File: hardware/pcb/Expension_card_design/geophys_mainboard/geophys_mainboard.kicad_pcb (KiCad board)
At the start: 4 copper layers, 190 x 110 mm, 297 parts, among them J1 550910274, J2 USB_C_Receptacle_USB2.0_16P, J3 550910274, J4 Micro_SD_CARD, Q1 AO3400A, Q2 AO3401A, Q3 AO3400A, U1 TPS61170, U10 TPS54331DR, U11 TPS7A2033PDBVR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

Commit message: SCL3300 driver functionnal
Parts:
- removed the D4 at (243.6, 58.8)
- removed D5, D6, D7: H5VUD5BB, Diode_SMD:D_SOD-523
- removed the Q1 at (211.8, 43.9)
- U9: value TPS25210LRPWR -> TPS2116DRL; footprint magnode_footprints:SMD_VQFN-HR-10 -> Package_TO_SOT_SMD:SOT-583-8
- moved U9 10.0 mm to (203.6, 77.5), turned to 0 degrees
- moved J2 0.11 mm to (236.6, 53.1)
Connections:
- D3 pad 1: /DATA_SAVING/CC2 -> /DATA_SAVING/+5VBUS
- D3 pad 3: /DATA_SAVING/CC1 -> /DATA_SAVING/D-
- D3 pad 4: unconnected-(D3-L3-Pad4) -> /DATA_SAVING/D+
- D3 pad 5: unconnected-(D3-L4-Pad5) -> /DATA_SAVING/CC1
- D3 pad 6: /DATA_SAVING/+5VBUS -> /DATA_SAVING/CC2
- J2 pad A5: /DATA_SAVING/CC1 -> /DATA_SAVING/CC2
- J2 pad B5: /DATA_SAVING/CC2 -> /DATA_SAVING/CC1
- U9 pad 1: /PWR_3V3D/3V3D_EFUSE_EN_ULVO -> unconnected-(U9-GND-Pad1)
- U9 pad 2: unconnected-(U9-OVCSEL-Pad2) -> Net-(U9-VOUT-Pad2)
- U9 pad 4: /PWR_3V3D/3V3D_EFUSE_PGTH -> unconnected-(U9-PR1-Pad4)
- U9 pad 5: /PWR_3V3D/+5V_IN -> unconnected-(U9-MODE-Pad5)
- U9 pad 6: /PWR_3V3D/5V_HOLDUP_DIODE -> unconnected-(U9-VIN2-Pad6)
- U9 pad 7: /PWR_3V3D/3V3D_EFUSE_DVDT -> Net-(U9-VOUT-Pad2)
- U9 pad 8: GND -> unconnected-(U9-ST-Pad8)
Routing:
- net /DATA_SAVING/CC2: track 12.9 -> 1.66 mm
- net /DATA_SAVING/D-: track 25.0 -> 16.5 mm, vias 2 -> 0
- net /DATA_SAVING/CC1: track 8.43 -> 1.65 mm
- net /DATA_SAVING/D+: track 23.3 -> 17.5 mm
- net /DATA_SAVING/+5VBUS: track 31.7 -> 26.8 mm, vias 6 -> 4
- net GND: track 89.3 -> 85.5 mm, vias 503 -> 494
- net unconnected-(J2-SBU2-PadB8): track 2.56 -> 0.00 mm, vias 1 -> 0

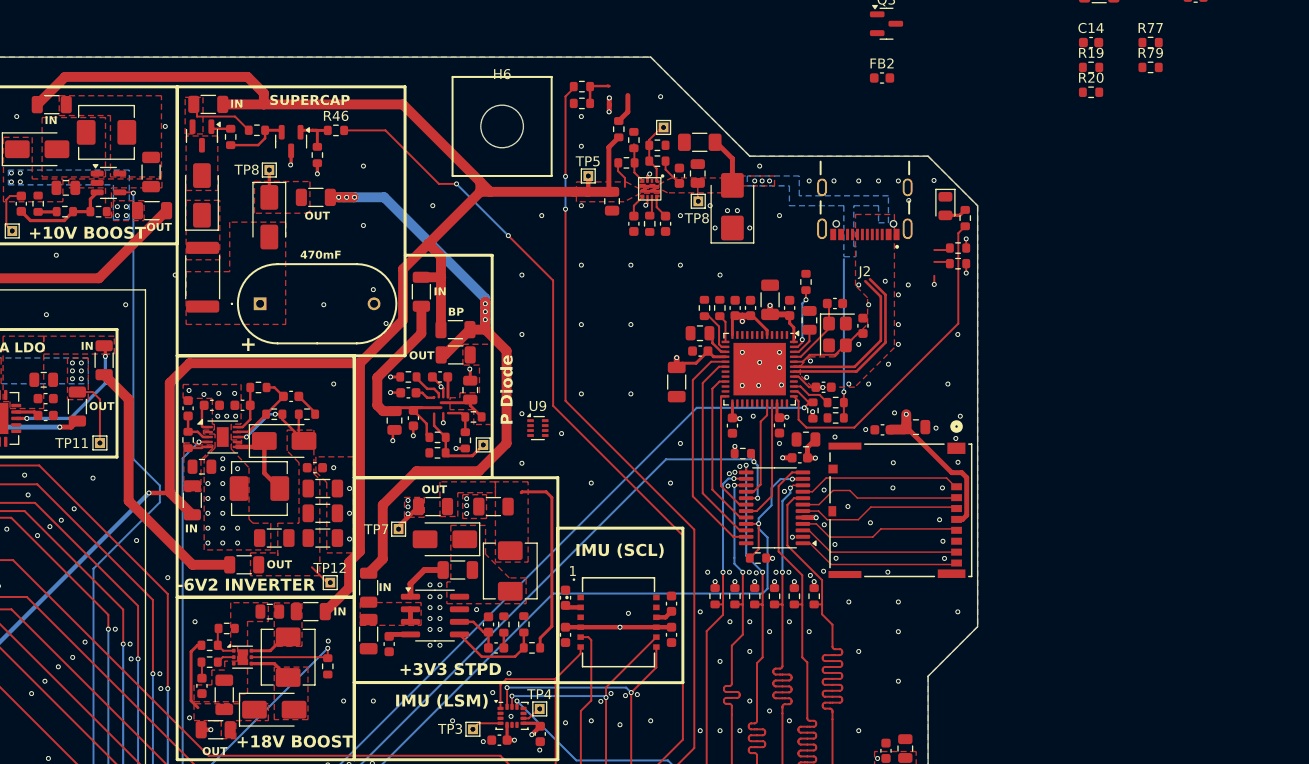
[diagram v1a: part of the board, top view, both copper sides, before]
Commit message: Backup avant deletion offset/dac
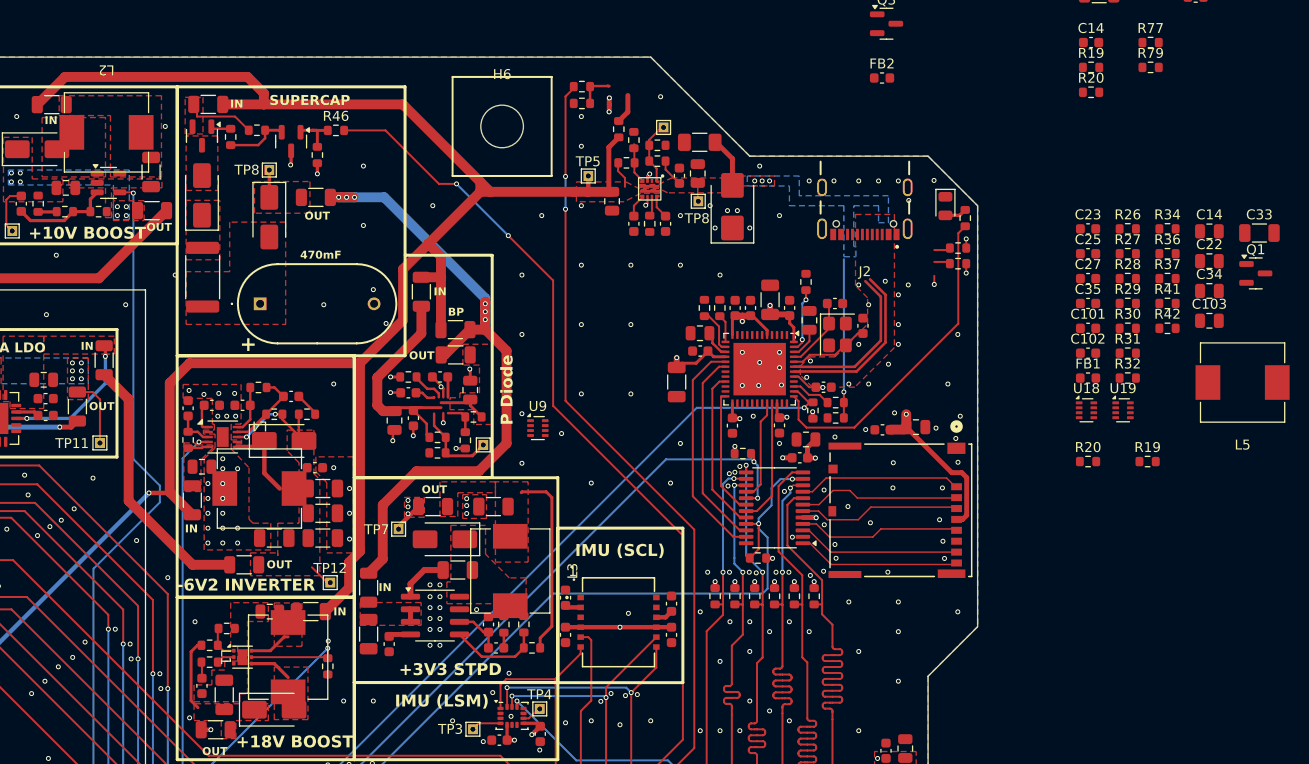
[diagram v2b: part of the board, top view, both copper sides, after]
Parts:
- added C101: 100n, Capacitor_SMD:C_0603_1608Metric, F.Cu at (259.1, 67.4)
- added C102: 100n, Capacitor_SMD:C_0603_1608Metric, F.Cu at (259.1, 69.9)
- added C103: 1u, Capacitor_SMD:C_0805_2012Metric, F.Cu at (271.4, 66.6)
- added C14: 1u, Capacitor_SMD:C_0805_2012Metric, F.Cu at (271.4, 57.6)
- added C22: 10u, Capacitor_SMD:C_0805_2012Metric, F.Cu at (271.4, 60.6)
- added C23: 100n, Capacitor_SMD:C_0603_1608Metric, F.Cu at (259.1, 57.3)
- added C25: 100n, Capacitor_SMD:C_0603_1608Metric, F.Cu at (259.1, 59.8)
- added C27: 15p, Capacitor_SMD:C_0603_1608Metric, F.Cu at (259.1, 62.4)
- added C33: 47u, Capacitor_SMD:C_1206_3216Metric, F.Cu at (276.4, 57.8)
- added C34: 10u, Capacitor_SMD:C_0805_2012Metric, F.Cu at (271.4, 63.6)
- added C35: 22n, Capacitor_SMD:C_0603_1608Metric, F.Cu at (259.1, 64.9)
- added FB1: 120Ω@100MHz 2A 50mΩ, Inductor_SMD:L_0603_1608Metric, F.Cu at (259.1, 72.4)
- added L5: 10u, magnode_footprints:ZEMS0850-100M_8.5x8.0mm, F.Cu at (274.8, 72.8)
- added Q1: AO3400A, Package_TO_SOT_SMD:SOT-23, F.Cu at (276.1, 61.8)
- added R19: 10k, Resistor_SMD:R_0603_1608Metric, F.Cu at (265.2, 80.8)
- added R20: 10k, Resistor_SMD:R_0603_1608Metric, F.Cu at (259.1, 80.8)
- added R26: 100, Resistor_SMD:R_0603_1608Metric, F.Cu at (263.2, 57.3)
- added R27: 100, Resistor_SMD:R_0603_1608Metric, F.Cu at (263.2, 59.8)
- added R28: 100k, Resistor_SMD:R_0603_1608Metric, F.Cu at (263.2, 62.4)
- added R29: 100k, Resistor_SMD:R_0603_1608Metric, F.Cu at (263.2, 64.9)
- added R30: 300k, Resistor_SMD:R_0603_1608Metric, F.Cu at (263.2, 67.4)
- added R31: 100k, Resistor_SMD:R_0603_1608Metric, F.Cu at (263.2, 69.9)
- added R32: 300k, Resistor_SMD:R_0603_1608Metric, F.Cu at (263.2, 72.4)
- added R34: 300k, Resistor_SMD:R_0603_1608Metric, F.Cu at (267.2, 57.3)
- added R36: ~, Resistor_SMD:R_0603_1608Metric, F.Cu at (267.2, 59.8)
- added R37: 300k, Resistor_SMD:R_0603_1608Metric, F.Cu at (267.2, 62.4)
- added R41: 100k, Resistor_SMD:R_0603_1608Metric, F.Cu at (267.2, 64.9)
- added R42: 100k, Resistor_SMD:R_0603_1608Metric, F.Cu at (267.2, 67.4)
- added U18: TPS2116DRL, Package_TO_SOT_SMD:SOT-583-8, F.Cu at (259.0, 75.7)
- added U19: TPS62933, Package_TO_SOT_SMD:SOT-583-8, F.Cu at (262.7, 75.7)
- L1, L2, L3, L4: footprint Inductor_SMD:L_Sunlord_MWSA0503S -> magnode_footprints:ZEMS0850-100M_8.5x8.0mm
- R64: value 27k -> 2k4
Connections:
- net /ADC_AD777x/PT1000_AIN+ renamed /ADC_AD777x/TH_AIN+
- net /ADC_AD777x/PT1000_AIN- renamed /ADC_AD777x/TH_AIN-
- net /ADC_AD777x/PT1000_DRAIN renamed /ADC_AD777x/TH_DRAIN
- net /PWR_3V3D/5V_SUPERCAP renamed /POWER/5V_SUPERCAP
- net /PWR_3V3D/STPD_3V3_BOOT renamed /POWER/STPD_3V3_BOOT
- net /PWR_3V3D/STPD_3V3_COMP renamed /POWER/STPD_3V3_COMP
- net /PWR_3V3D/STPD_3V3_COMP_F renamed /POWER/STPD_3V3_COMP_F
- net /PWR_3V3D/STPD_3V3_PH renamed /POWER/STPD_3V3_PH
- net /PWR_3V3D/STPD_3V3_SS renamed /POWER/STPD_3V3_SS
- net /PWR_3V3D/STPD_3V3_VSENS renamed /POWER/STPD_3V3_VSENS
- C28 pad 1: /PWR_3V3D/5V_HOLDUP_IN -> /POWER/5V_STEP_DOWN_IN
- C29 pad 1: /PWR_3V3D/+3V3_OUT -> +3V3
- D9 pad 1: Net-(D9-K) -> /POWER/5V_HOLDUP_CAP
- L3 pad 2: /PWR_3V3D/+3V3_OUT -> +3V3
- Q2 pad 2: /PWR_3V3D/+5V_SUPERCAP_IN -> +5V
- R15 pad 1: +5V -> /PWR_9V_BRIDGE/+5V
- R38 pad 1: /PWR_3V3D/+3V3_OUT -> +3V3
- R44 pad 1: /PWR_3V3D/+5V_SUPERCAP_IN -> +5V
- R50 pad 1: +5V -> /PWR_3V3A/+5V
- R91 pad 1: +5V -> /DATA_SAVING/+5VBUS
- U10 pad 2: /PWR_3V3D/5V_HOLDUP_IN -> /POWER/5V_STEP_DOWN_IN
- U10 pad 3: /PWR_3V3D/5V_HOLDUP_IN -> /POWER/5V_STEP_DOWN_IN
- U4 pad 7: /IO_CONNECTOR/EN_KEEPALIVE -> /MCU_ESP32S3/EN_KEEPALIVE
- U5 pad 10: /IMU/CS_LSM -> /IMU/SCLK
- U5 pad 11: /MCU_ESP32S3/EN_SUPERCAP_CHARGE -> /IMU/MOSI
- U5 pad 12: /IMU/MOSI -> /DEVICE_DETECT_2
- U5 pad 13: /IMU/SCLK -> /DEVICE_DETECT_1
- U5 pad 28: /DEVICE_DETECT_2 -> /MCU_ESP32S3/EN_SUPERCAP_CHARGE
- U5 pad 31: /DEVICE_DETECT_1 -> unconnected-(U5-GPIO39-Pad31)
- U9 pad 1: unconnected-(U9-GND-Pad1) -> GND
- U9 pad 2: Net-(U9-VOUT-Pad2) -> /POWER/5V_STEP_DOWN_IN
- U9 pad 3: unconnected-(U9-VIN1-Pad3) -> +5V
- U9 pad 4: unconnected-(U9-PR1-Pad4) -> Net-(U9-PR1)
- U9 pad 5: unconnected-(U9-MODE-Pad5) -> +5V
- U9 pad 6: unconnected-(U9-VIN2-Pad6) -> /POWER/5V_HOLDUP_CAP
- U9 pad 7: Net-(U9-VOUT-Pad2) -> /POWER/5V_STEP_DOWN_IN
- U9 pad 8: unconnected-(U9-ST-Pad8) -> /POWER/5V_USB_PRESENT
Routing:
- net +3V3: track 446.6 -> 465.6 mm
- net /PWR_3V3D/+3V3_OUT: track 19.0 -> 0.00 mm
- net /PWR_3V3D/5V_HOLDUP_IN: track 1.36 -> 0.00 mm
- net /POWER/5V_STEP_DOWN_IN: track 0.00 -> 1.36 mm
- added copper zone on F.Cu, net /POWER/5V_HOLDUP_CAP
- added copper zone on F.Cu, net /POWER/5V_STEP_DOWN_IN
- removed copper zone on F.Cu, net /PWR_3V3D/+3V3_OUT
- removed copper zone on F.Cu, net /PWR_3V3D/+5V_SUPERCAP_IN
- removed copper zone on F.Cu, net /PWR_3V3D/5V_HOLDUP_IN
- removed copper zone on F.Cu, net Net-(D9-K)

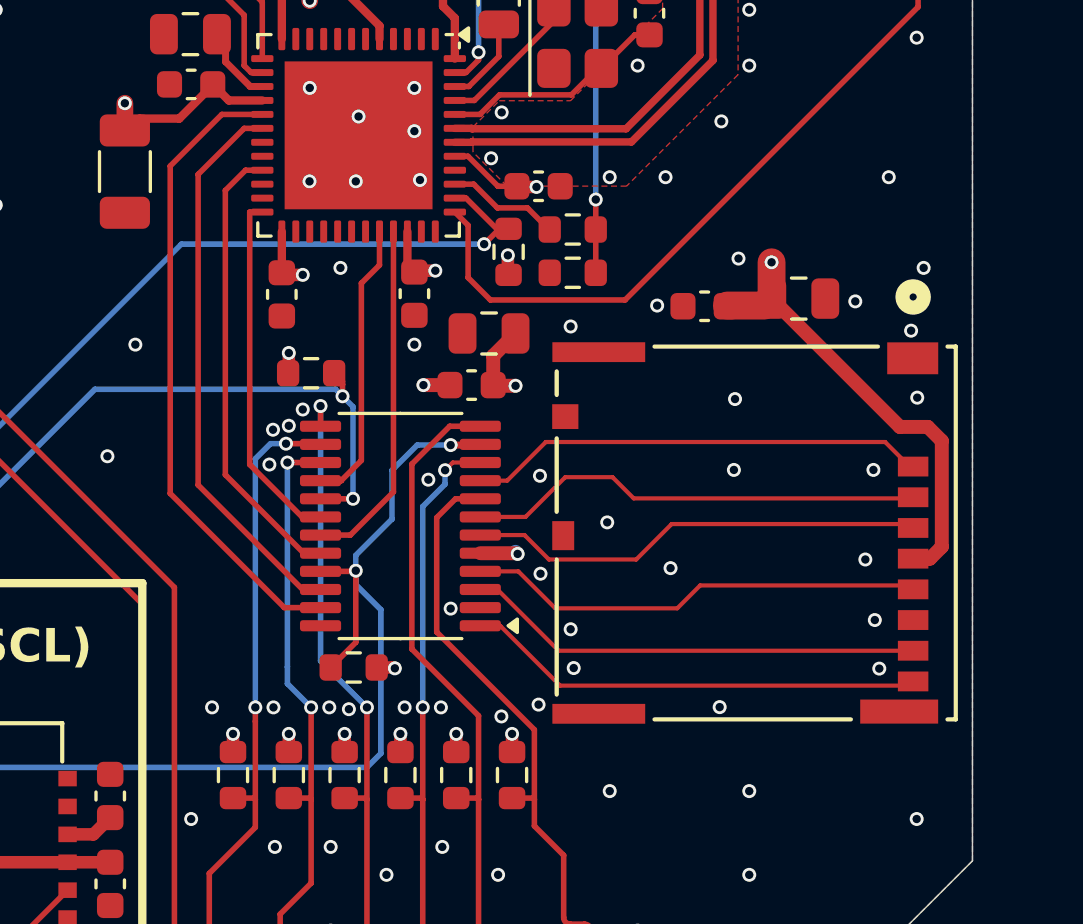
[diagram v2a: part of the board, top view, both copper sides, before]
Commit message: SD mux and 3V3D power sequencing bring-up
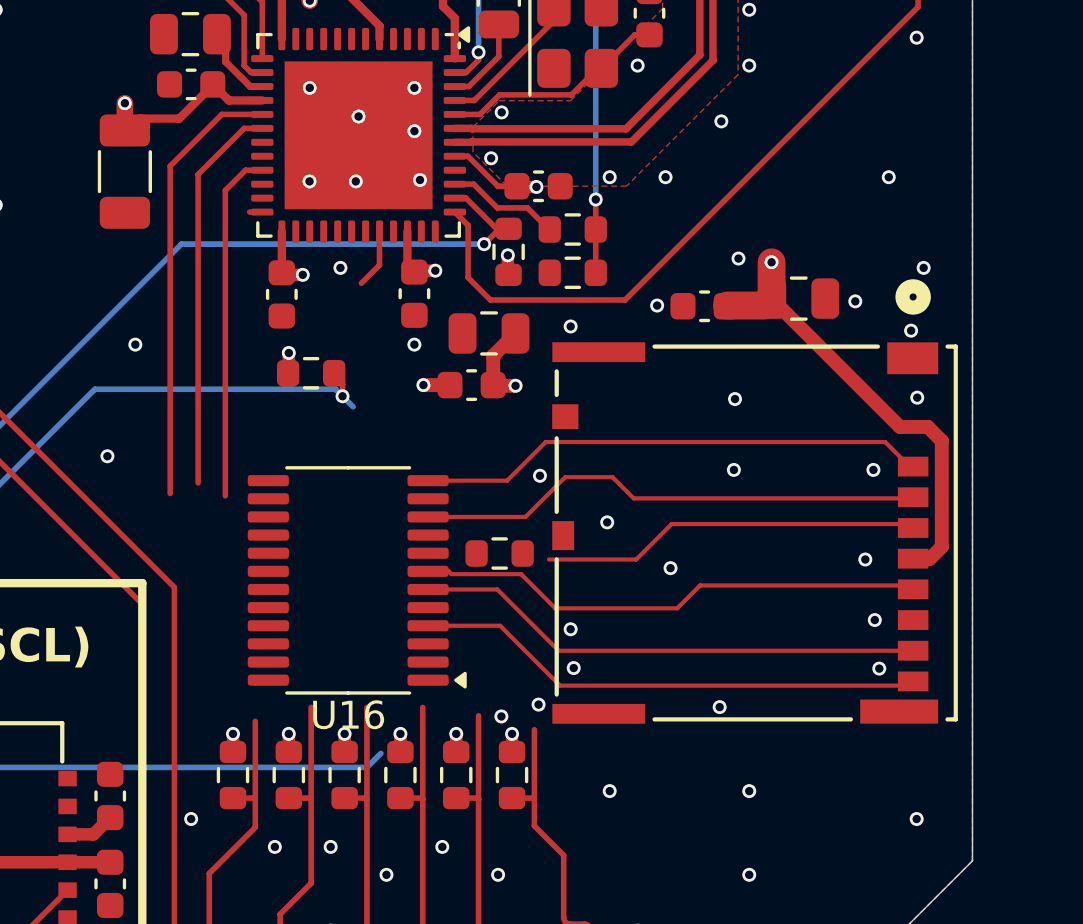
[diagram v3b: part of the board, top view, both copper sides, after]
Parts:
- moved R95 6.64 mm to (231.1, 86.5), turned to 0 degrees
- moved U16 2.70 mm to (225.6, 87.5)
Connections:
- U16 pad 1: /DATA_SAVING/MD1 -> /DATA_SAVING/E_D0
- U16 pad 10: /DATA_SAVING/E_D0 -> /DATA_SAVING/MD3
- U16 pad 11: /DATA_SAVING/SD_MUX_SEL -> /DATA_SAVING/USB_D1
- U16 pad 12: /DATA_SAVING/E_CLK -> /DATA_SAVING/MD2
- U16 pad 13: /DATA_SAVING/E_D2 -> /DATA_SAVING/USB_D0
- U16 pad 14: /DATA_SAVING/E_CMD -> /DATA_SAVING/SD_MUX_SEL
- U16 pad 15: /DATA_SAVING/E_D3 -> /DATA_SAVING/USB_CLK
- U16 pad 16: /DATA_SAVING/USB_D3 -> /DATA_SAVING/USB_D2
- U16 pad 17: /DATA_SAVING/EN_SD_MUX -> /DATA_SAVING/USB_CMD
- U16 pad 18: /DATA_SAVING/USB_CMD -> /DATA_SAVING/USB_D3
- U16 pad 19: /DATA_SAVING/USB_D2 -> /DATA_SAVING/E_D3
- U16 pad 2: GND -> /DATA_SAVING/E_D1
- U16 pad 20: /DATA_SAVING/USB_CLK -> /DATA_SAVING/EN_SD_MUX
- U16 pad 21: /DATA_SAVING/SD_MUX_SEL -> /DATA_SAVING/E_CMD
- U16 pad 22: /DATA_SAVING/USB_D0 -> /DATA_SAVING/E_D2
- U16 pad 23: /DATA_SAVING/USB_D1 -> /DATA_SAVING/E_CLK
- U16 pad 24: unconnected-(U16-N.C.-Pad24) -> /DATA_SAVING/SD_MUX_SEL
- U16 pad 3: /DATA_SAVING/MD0 -> unconnected-(U16-N.C.-Pad3)
- U16 pad 4: /DATA_SAVING/MCLK -> /DATA_SAVING/MD1
- U16 pad 5: +3V3 -> GND
- U16 pad 6: /DATA_SAVING/MCMD -> /DATA_SAVING/MD0
- U16 pad 7: /DATA_SAVING/MD3 -> /DATA_SAVING/MCLK
- U16 pad 8: /DATA_SAVING/E_D1 -> +3V3
- U16 pad 9: /DATA_SAVING/MD2 -> /DATA_SAVING/MCMD
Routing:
- net /DATA_SAVING/SD_MUX_SEL: track 96.8 -> 77.1 mm, vias 3 -> 1
- net /DATA_SAVING/E_CLK: track 47.6 -> 34.6 mm
- net /DATA_SAVING/USB_D2: track 12.6 -> 0.00 mm
- net /DATA_SAVING/USB_CMD: track 12.8 -> 0.45 mm
- net /DATA_SAVING/E_D2: track 41.8 -> 29.6 mm, vias 2 -> 0
- net /DATA_SAVING/E_CMD: track 34.6 -> 22.6 mm, vias 2 -> 0
- net /DATA_SAVING/E_D1: track 50.1 -> 39.2 mm
- net /DATA_SAVING/E_D3: track 37.0 -> 26.7 mm, vias 2 -> 0
- net /DATA_SAVING/E_D0: track 42.0 -> 31.8 mm, vias 2 -> 0
- net /DATA_SAVING/USB_D3: track 11.0 -> 2.12 mm
- net /DATA_SAVING/USB_D1: track 22.9 -> 15.8 mm
- net /DATA_SAVING/USB_D0: track 20.1 -> 14.0 mm
- net /DATA_SAVING/EN_SD_MUX: track 97.1 -> 92.6 mm, vias 3 -> 2
- net /DATA_SAVING/USB_CLK: track 16.4 -> 12.6 mm
- net /DATA_SAVING/MCMD: track 16.4 -> 13.6 mm
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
